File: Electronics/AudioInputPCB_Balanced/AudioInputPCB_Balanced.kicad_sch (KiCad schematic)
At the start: 110 parts, among them J1 IDC, J2 IDC, J3 XLR3_Ground, J4 XLR3_Ground, J5 XLR3_Ground, J6 XLR3_Ground, U1 NE5532, U2 NE5532, U3 NE5532, U4 NE5532

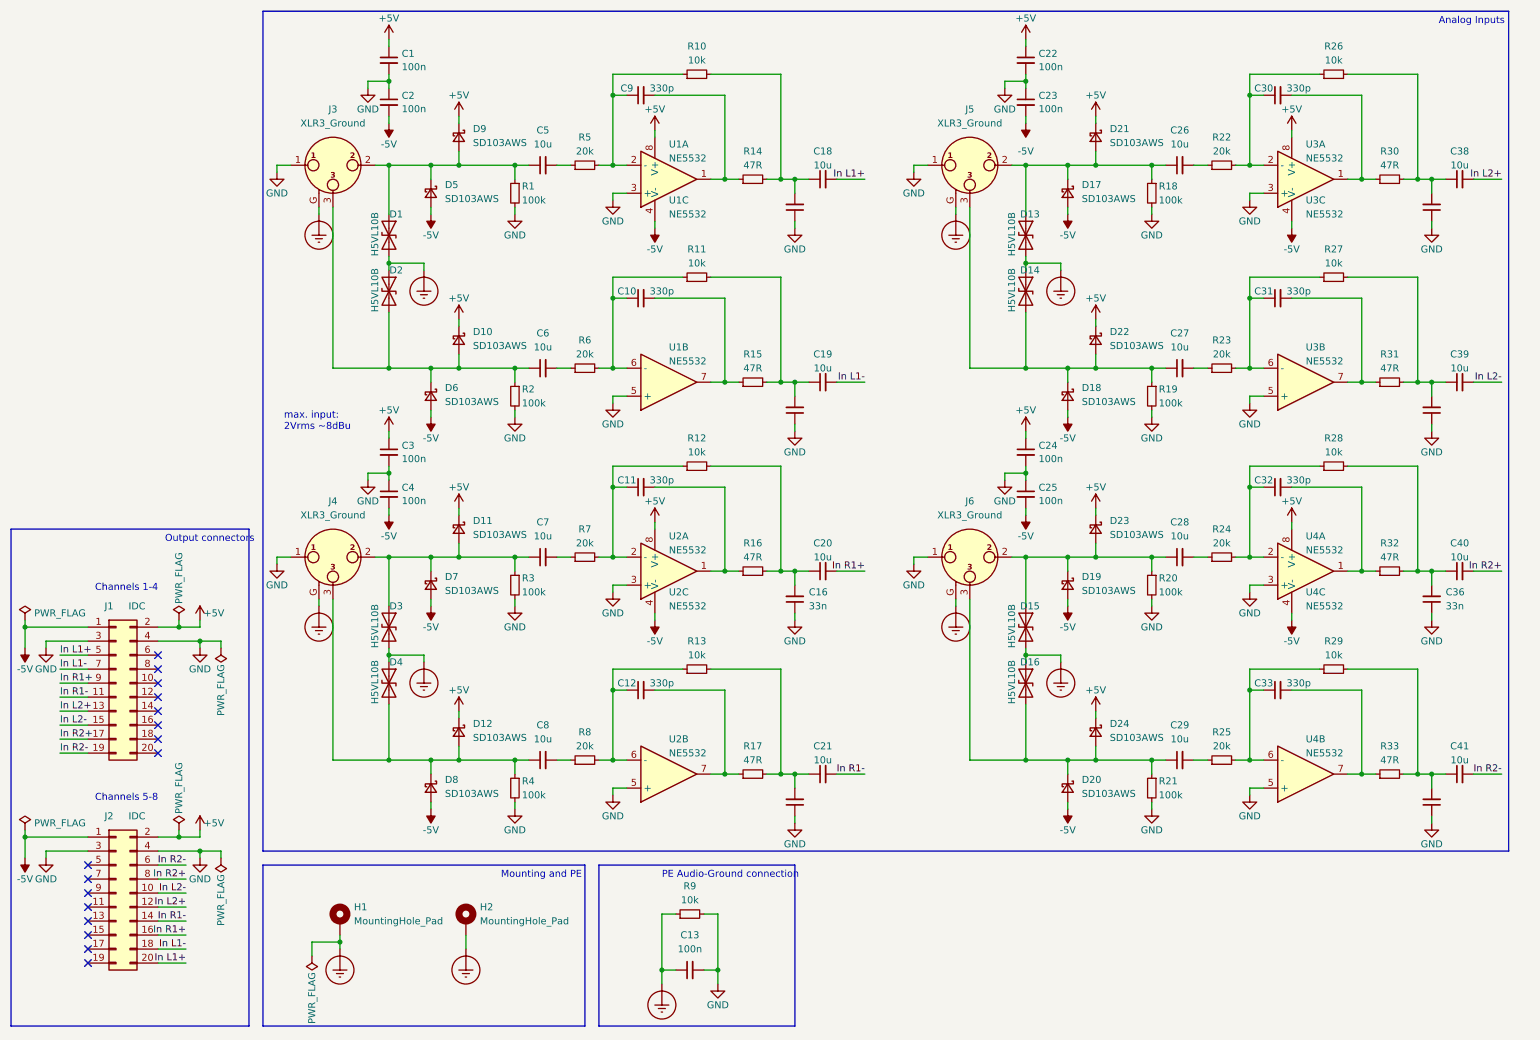
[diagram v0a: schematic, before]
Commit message: Final commit before fabrication of: Maxi, Unbal In and Unbal Out Rev1.0
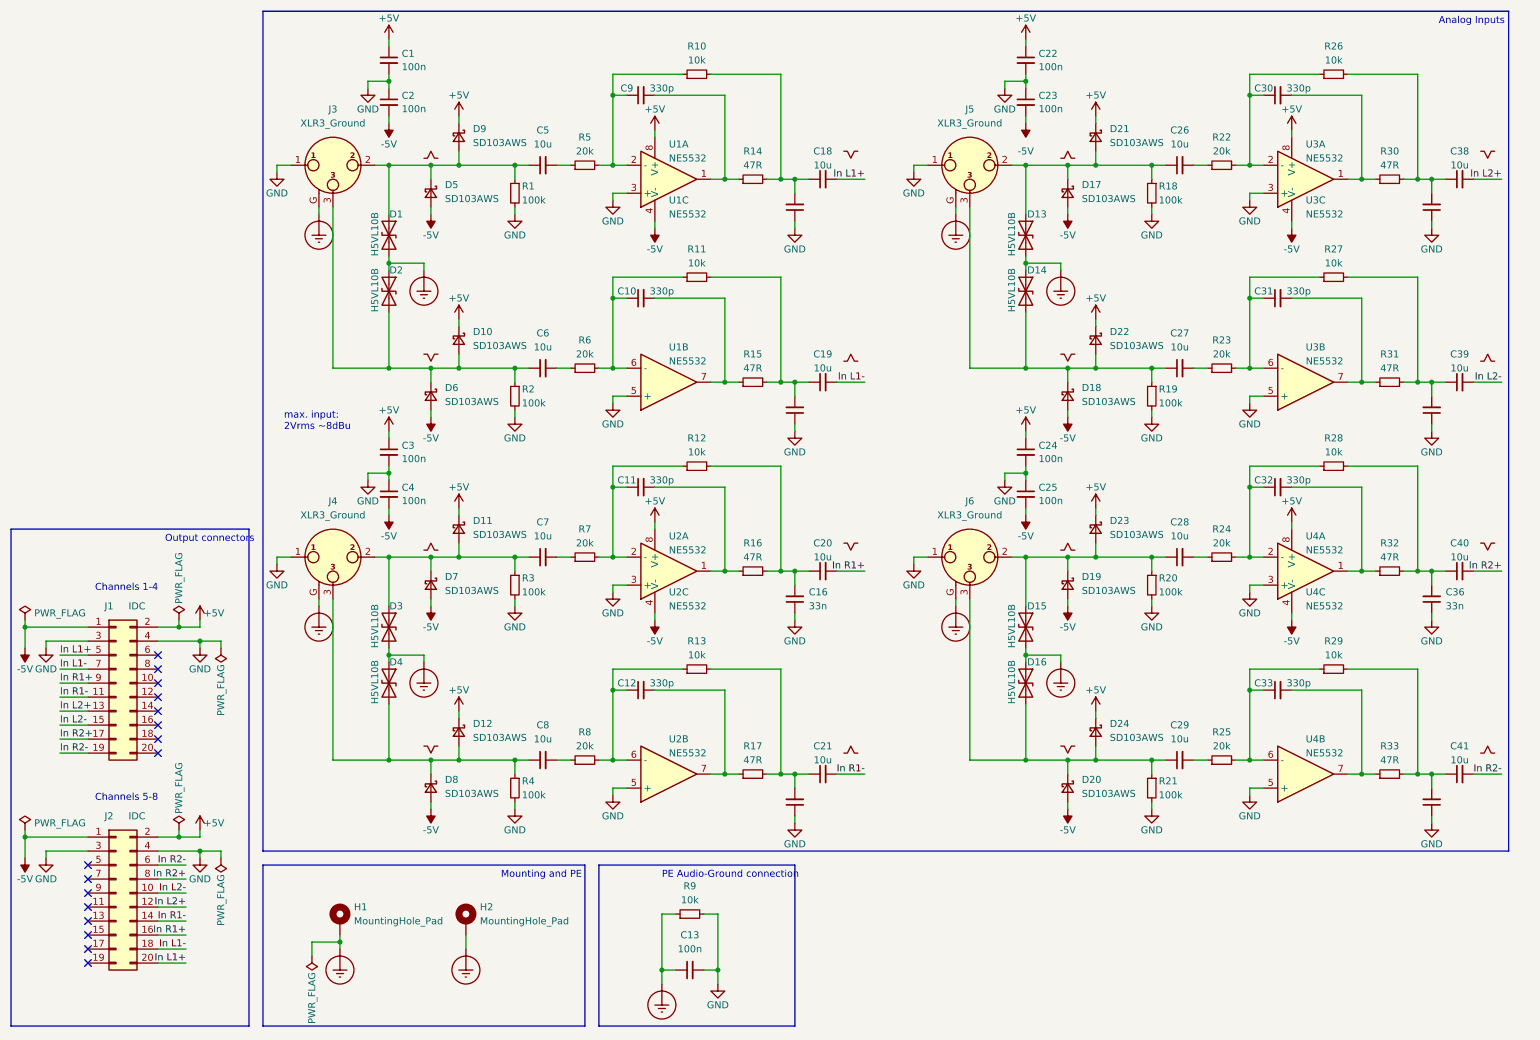
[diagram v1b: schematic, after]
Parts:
- added S1, S10, S11, S12, S13, S14, S15, S16, S2, S3, S4, S5, S6, S7, S8, S9: Phase, symbol 1_Project_Symbols:Phase
